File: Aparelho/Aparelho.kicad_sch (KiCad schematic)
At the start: 11 parts

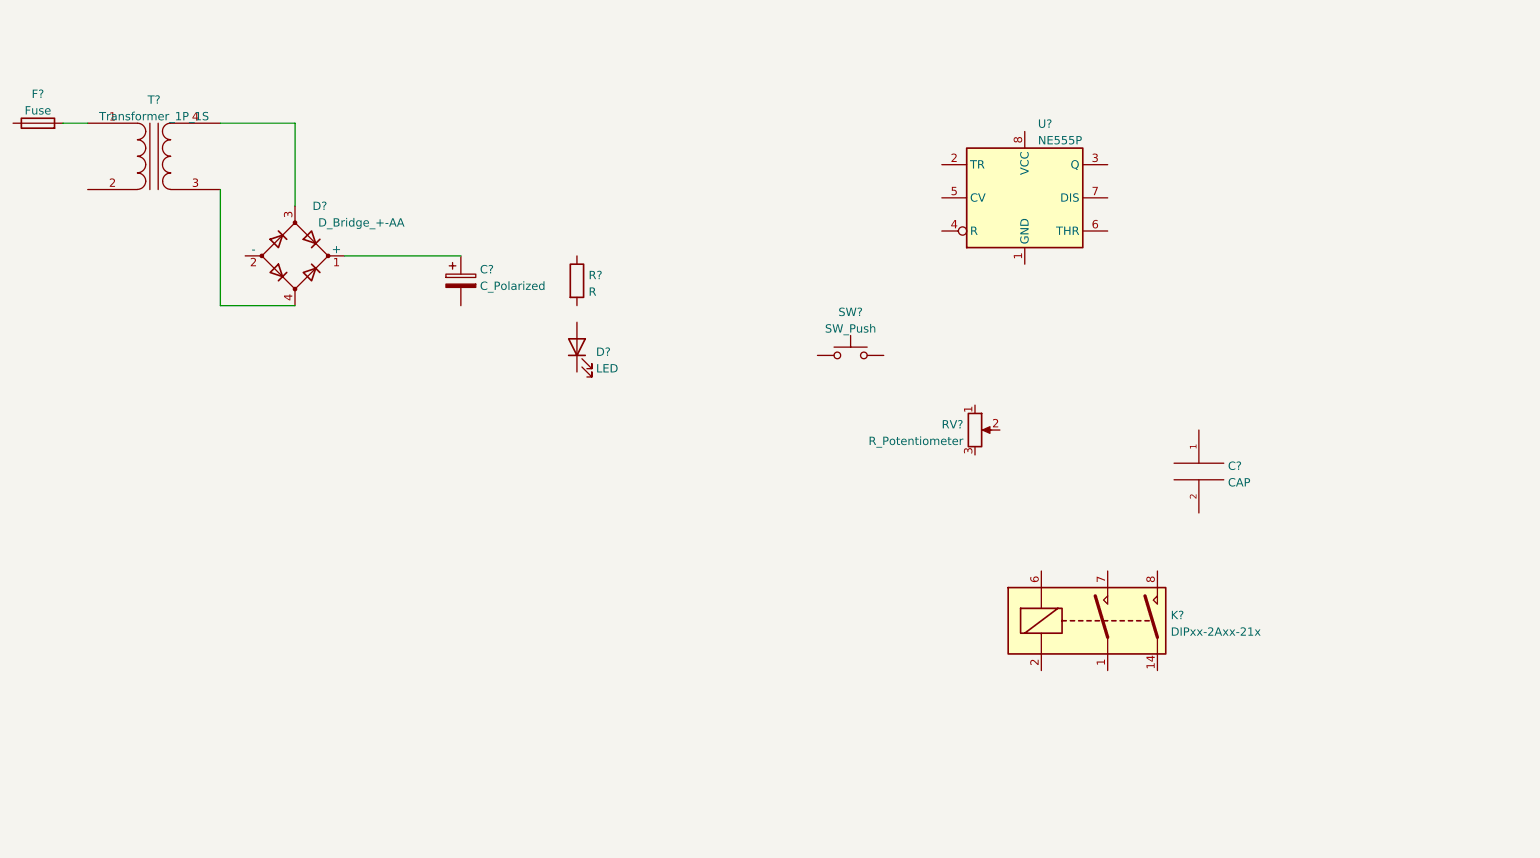
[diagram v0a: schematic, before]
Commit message: connected all the components and put their values
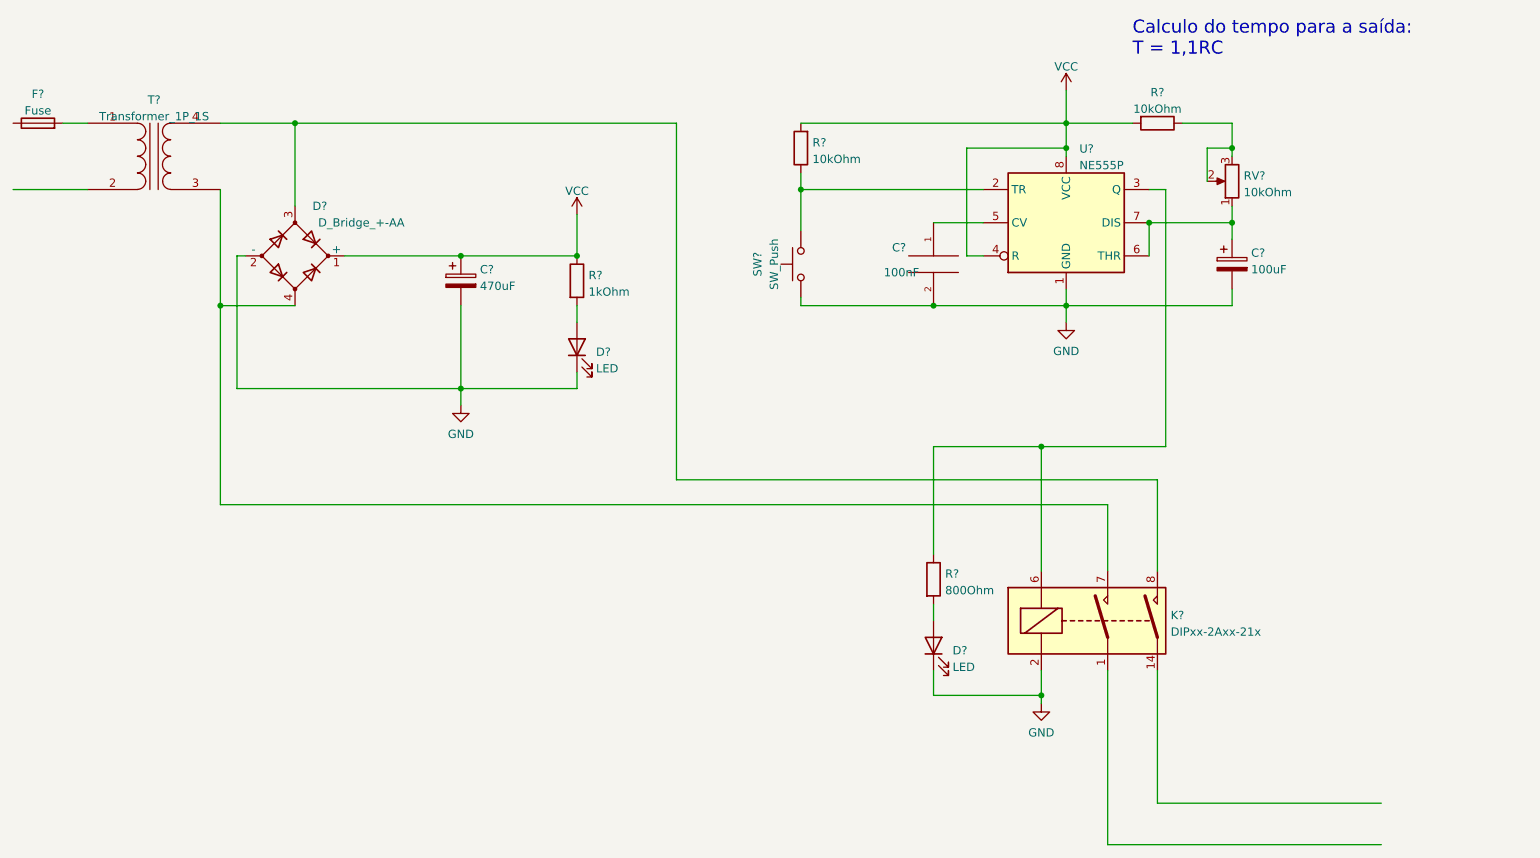
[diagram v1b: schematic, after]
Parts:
- added C?: 100uF, symbol Device:C_Polarized
- added D?: LED, symbol Device:LED
- added R? (x2): 10kOhm, symbol Device:R
- added R?: 800Ohm, symbol Device:R
- C?: value CAP -> 100nF
- C?: value C_Polarized -> 470uF
- R?: value R -> 1kOhm
- RV?: value R_Potentiometer -> 10kOhm
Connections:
- net at D?.4, T?.3 (SA): now also K?.7
- net at D?.3, T?.4 (SB): now also K?.8
- net VCC: now reaches R?.1
- net VCC: now also C?.1, D?.1 (+), U?.4 (R), U?.8 (VCC), R?.2, R?.2
- net at R?.2: now also D?.2 (A)
- net at C?.1: now also U?.5 (CV)
- net GND: now reaches C?.2
- net GND: now also C?.2, D?.1 (K), D?.2 (-), K?.2, SW?.1, U?.1 (GND), C?.2, D?.1 (K)
- net at SW?.2: now also U?.2 (TR), R?.1
- net at RV?.1: now also U?.6 (THR), U?.7 (DIS), C?.1
- net at RV?.2: now also RV?.3, R?.1
- net at K?.6: now also U?.3 (Q), R?.1
- new net: D?.2 (A), R?.2
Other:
- note added: "Calculo do tempo para a saída: T = 1,1RC"
- moved on the sheet: C?, RV?, SW?, U?
